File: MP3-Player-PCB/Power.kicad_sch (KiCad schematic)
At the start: 43 parts, among them J201 Conn_01x02_Socket, J202 USB_C_Receptacle_USB2.0_16P, U201 BQ24259, U202 USBLC6-2SC6, U203 TPS7A2033PDBVR, U204 TPS7A2033PDBVR

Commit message: Fixed all ERC errors
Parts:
- renumbered C216 to C212, C217 to C213, C212 to C214, C213 to C215, C214 to C216, C215 to C217, R215 to R214, R214 to R215
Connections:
- net +VSYS: no longer C213.1, C214.1, FB201.2, U203.1 (IN), U203.3 (EN)
- new net +VSYS_FILT: C213.1, C214.1, FB201.2, U203.1 (IN), U203.3 (EN)

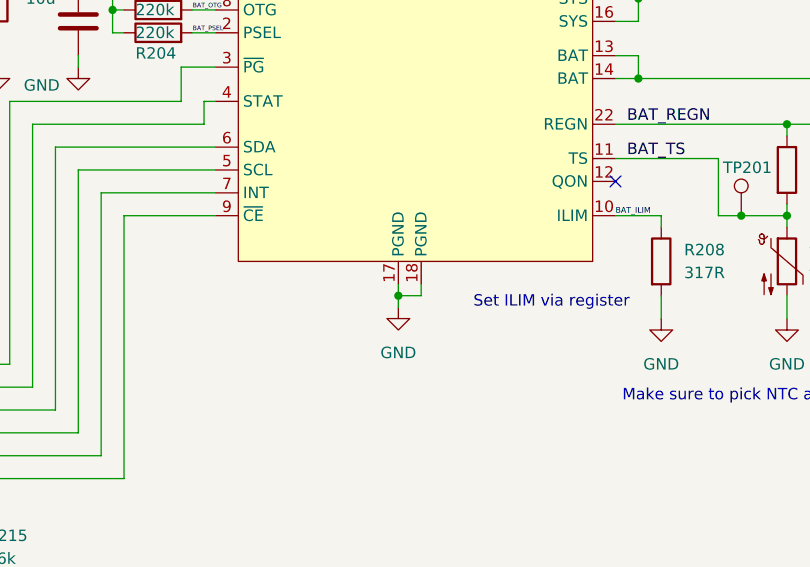
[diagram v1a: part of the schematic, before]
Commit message: Fixed all import change from schematic errors and warnings
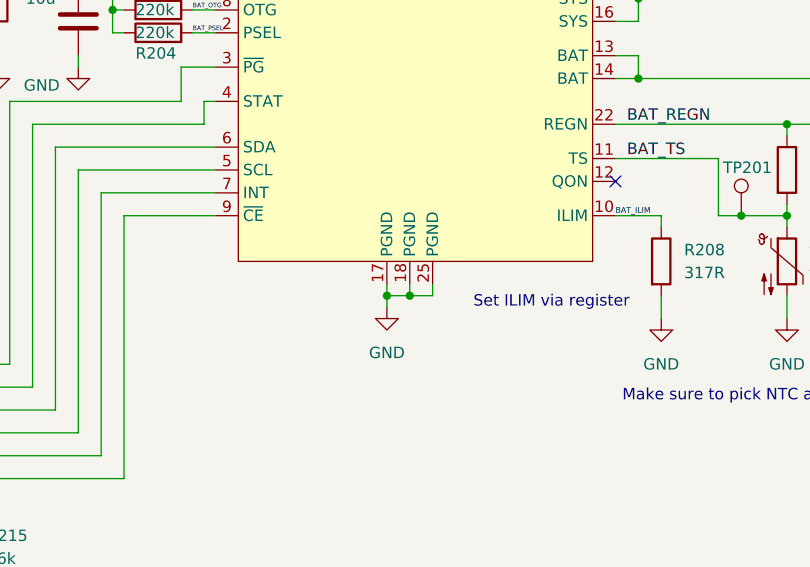
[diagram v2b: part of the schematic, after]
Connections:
- net GND: now also U201.25 (PGND)
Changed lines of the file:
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@@
 	)
 	(junction
-		(at 148.59 73.66)
+		(at 147.32 73.66)
 		(diameter 0)
 		(color 0 0 0 0)
@@
 	)
 	(junction
+		(at 149.86 73.66)
+		(diameter 0)
+		(color 0 0 0 0)
+	)
+	(junction
 		(at 73.66 71.12)
 		(diameter 0)
@@
 	(wire
 		(pts
-			(xy 148.59 73.66) (xy 148.59 74.93)
+			(xy 147.32 73.66) (xy 147.32 74.93)
 		)
 		(stroke
@@
 	(wire
 		(pts
+			(xy 152.4 72.39) (xy 152.4 73.66)
+		)
+		(stroke
+			(width 0)
+			(type default)
+		)
+	)
+	(wire
+		(pts
 			(xy 118.11 44.45) (xy 116.84 44.45)
 		)
@@
 	(wire
 		(pts
-			(xy 151.13 73.66) (xy 148.59 73.66)
+			(xy 149.86 73.66) (xy 147.32 73.66)
 		)
 		(stroke
@@
 	(wire
 		(pts
-			(xy 148.59 72.39) (xy 148.59 73.66)
+			(xy 147.32 72.39) (xy 147.32 73.66)
 		)
 		(stroke
@@
 	(wire
 		(pts
-			(xy 151.13 72.39) (xy 151.13 73.66)
+			(xy 149.86 72.39) (xy 149.86 73.66)
 		)
 		(stroke
@@
 	(wire
 		(pts
+			(xy 152.4 73.66) (xy 149.86 73.66)
+		)
+		(stroke
+			(width 0)
+			(type default)
+		)
+	)
+	(wire
+		(pts
 			(xy 186.69 30.48) (xy 190.5 30.48)
 		)
@@
 		(pin "2"
 		)
+		(pin "25"
+		)
 		(instances
 			(project ""
@@
 	(symbol
 		(lib_id "power:GND")
-		(at 148.59 74.93 0)
+		(at 147.32 74.93 0)
 		(unit 1)
 		(exclude_from_sim no)
@@
 		(fields_autoplaced yes)
 		(property "Reference" "#PWR0217"
-			(at 148.59 81.28 0)
+			(at 147.32 81.28 0)
 			(effects
 				(font
@@
 		)
 		(property "Value" "GND"
-			(at 148.59 80.01 0)
+			(at 147.32 80.01 0)
 			(effects
 				(font
@@
 		)
 		(property "Footprint" ""
-			(at 148.59 74.93 0)
+			(at 147.32 74.93 0)
 			(effects
 				(font
@@
 		)
 		(property "Datasheet" ""
-			(at 148.59 74.93 0)
+			(at 147.32 74.93 0)
 			(effects
 				(font
@@
 		)
 		(property "Description" "Power symbol creates a global label with name \"GND\" , ground"
-			(at 148.59 74.93 0)
+			(at 147.32 74.93 0)
 			(effects
 				(font

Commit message: Much better initial layout
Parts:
- C201, C202, C204: footprint Capacitor_SMD:C_0603_1608Metric -> Capacitor_SMD:C_0402_1005Metric
- C203, C209, C211, C212, C213: footprint Capacitor_SMD:C_0805_2012Metric -> Capacitor_SMD:C_0603_1608Metric
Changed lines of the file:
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@@
 			)
 		)
-		(property "Footprint" "Capacitor_SMD:C_0805_2012Metric"
+		(property "Footprint" "Capacitor_SMD:C_0603_1608Metric"
 			(at 44.1452 148.59 0)
 			(effects
@@
 			)
 		)
-		(property "Footprint" "Capacitor_SMD:C_0805_2012Metric"
+		(property "Footprint" "Capacitor_SMD:C_0603_1608Metric"
 			(at 26.3652 148.59 0)
 			(effects
@@
 			)
 		)
-		(property "Footprint" "Capacitor_SMD:C_0805_2012Metric"
+		(property "Footprint" "Capacitor_SMD:C_0603_1608Metric"
 			(at 113.9952 46.99 0)
 			(effects
@@
 			)
 		)
-		(property "Footprint" "Capacitor_SMD:C_0805_2012Metric"
+		(property "Footprint" "Capacitor_SMD:C_0603_1608Metric"
 			(at 213.0552 64.77 0)
 			(effects
@@
 			)
 		)
-		(property "Footprint" "Capacitor_SMD:C_0805_2012Metric"
+		(property "Footprint" "Capacitor_SMD:C_0603_1608Metric"
 			(at 96.2152 40.64 0)
 			(effects
@@
 			)
 		)
-		(property "Footprint" "Capacitor_SMD:C_0603_1608Metric"
+		(property "Footprint" "Capacitor_SMD:C_0402_1005Metric"
 			(at 68.2752 40.64 0)
 			(effects
@@
 			)
 		)
-		(property "Footprint" "Capacitor_SMD:C_0603_1608Metric"
+		(property "Footprint" "Capacitor_SMD:C_0402_1005Metric"
 			(at 182.88 35.8648 0)
 			(effects
@@
 			)
 		)
-		(property "Footprint" "Capacitor_SMD:C_0603_1608Metric"
+		(property "Footprint" "Capacitor_SMD:C_0402_1005Metric"
 			(at 84.7852 40.64 0)
 			(effects

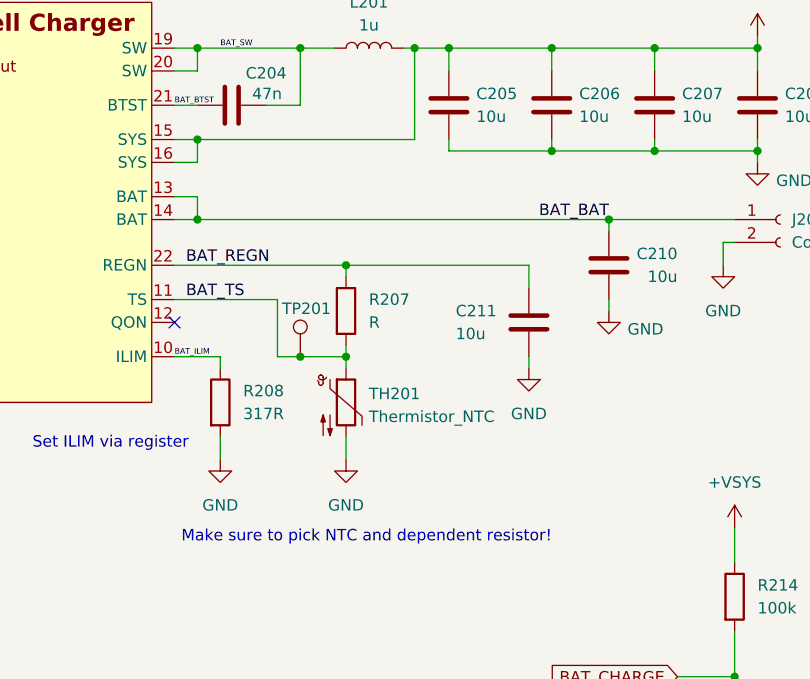
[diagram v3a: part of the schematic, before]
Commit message: Routing more mcu signals
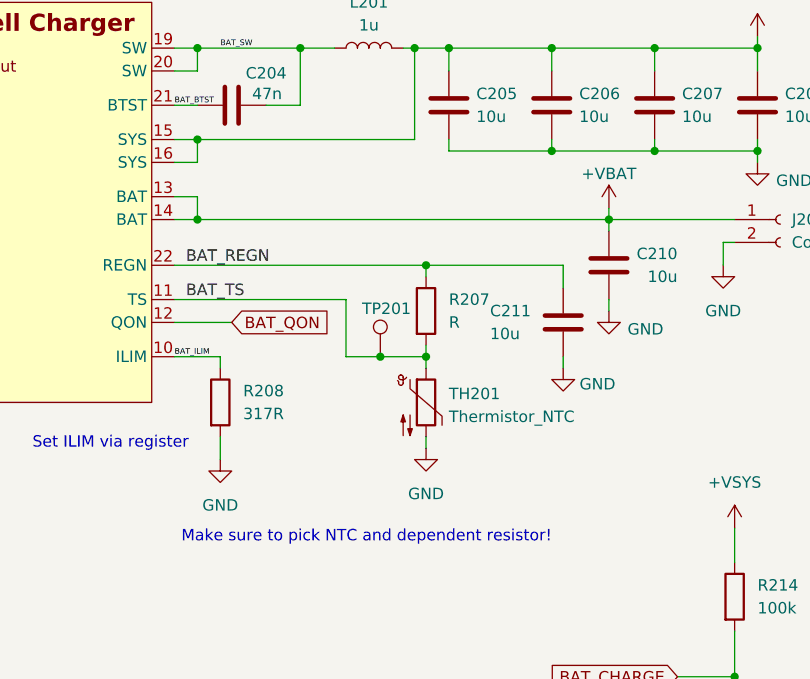
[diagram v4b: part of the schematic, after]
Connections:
- net BAT_QON: now reaches U201.12 (QON)
- net BAT_BAT renamed +VBAT
- no-connect marks 3 -> 2
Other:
- moved on the sheet: C211, R207, TH201, TP201

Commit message: Changing JST connector footprint to fit next to usb
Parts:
- J201: footprint Connector_JST:JST_EH_S2B-EH_1x02_P2.50mm_Horizontal -> Connector_JST:JST_GH_SM02B-GHS-TB_1x02-1MP_P1.25mm_Horizontal
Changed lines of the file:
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@@
 			)
 		)
-		(property "Footprint" "Connector_JST:JST_EH_S2B-EH_1x02_P2.50mm_Horizontal"
+		(property "Footprint" "Connector_JST:JST_GH_SM02B-GHS-TB_1x02-1MP_P1.25mm_Horizontal"
 			(at 240.03 49.53 0)
 			(effects

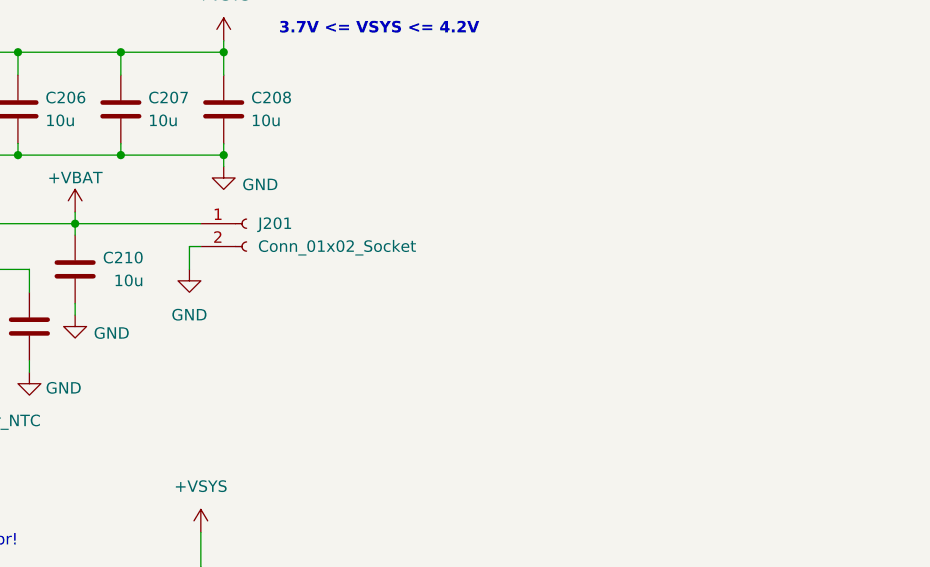
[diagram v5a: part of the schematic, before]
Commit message: Routed VBAT power trace in 3rd layer
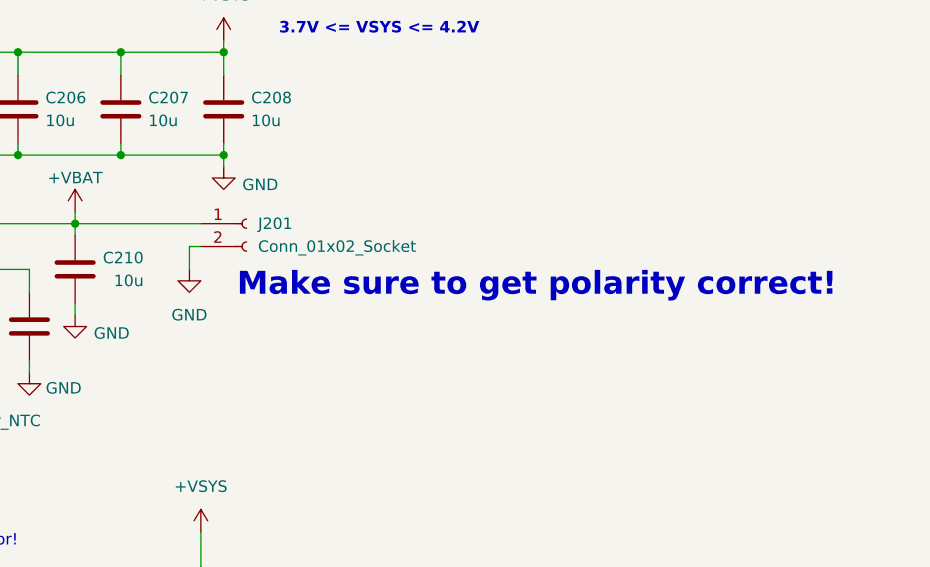
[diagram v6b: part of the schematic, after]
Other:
- note added: "Make sure to get polarity correct!"
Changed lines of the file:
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@@
+		)
+	)
+	(text "Make sure to get polarity correct!"
+		(exclude_from_sim no)
+		(at 272.288 56.388 0)
+		(effects
+			(font
+				(size 2.54 2.54)
+				(thickness 0.254)
+				(bold yes)
+			)
 		)
 	)

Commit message: Assigning JLCPCB part #'s
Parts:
- C201, C202: JLCPCB Part # (none) -> C1525
- C203, C209, C211, C212, C213: JLCPCB Part # (none) -> C19702
- C204: JLCPCB Part # (none) -> C82219
- C205, C206, C207, C208, C210, C214, C215, C216, C217: JLCPCB Part # (none) -> C15850
- FB201: JLCPCB Part # (none) -> C5671
- J201: JLCPCB Part # (none) -> C189893
- J202: footprint Connector_USB:USB_C_Receptacle_GCT_USB4105-xx-A_16P_TopMnt_Horizontal -> Connector_USB:USB_C_Receptacle_HRO_TYPE-C-31-M-12; JLCPCB Part # (none) -> C165948
- L201: JLCPCB Part # (none) -> C43388
- R201: JLCPCB Part # (none) -> C15402
- R202, R203, R204: JLCPCB Part # (none) -> C25546
- R205, R206: JLCPCB Part # (none) -> C25905
- R209, R210, R213, R215: JLCPCB Part # (none) -> C25796
- R211, R212: JLCPCB Part # (none) -> C25531
- R214: JLCPCB Part # (none) -> C25741
- R216: JLCPCB Part # (none) -> C25764
- TH201: JLCPCB Part # (none) -> C700814
- TP201: now left out of the parts list
- U201: JLCPCB Part # (none) -> C473366
- U202: JLCPCB Part # (none) -> C7519
- U203, U204: JLCPCB Part # (none) -> C2862740

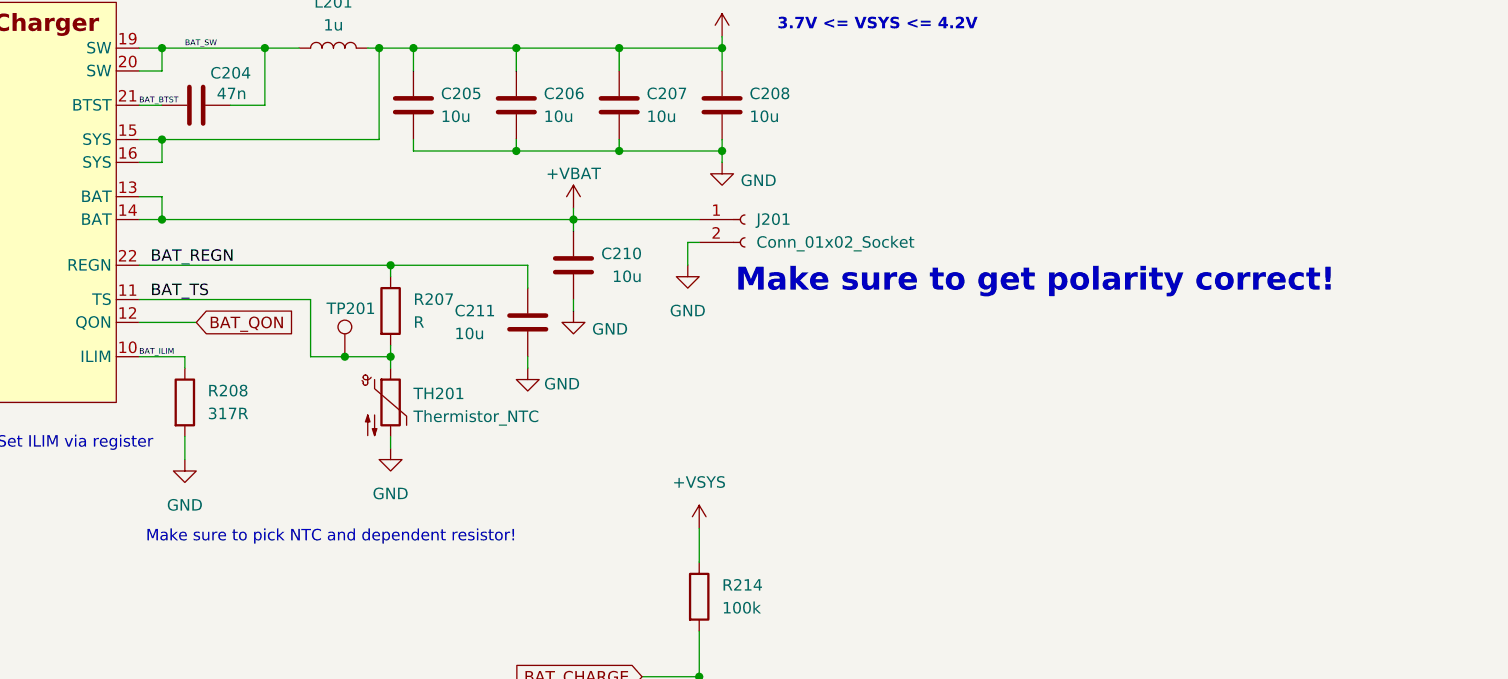
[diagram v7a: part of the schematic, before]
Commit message: Added 5.25k resistor to thermistor divider network as per BQ24259 datasheet
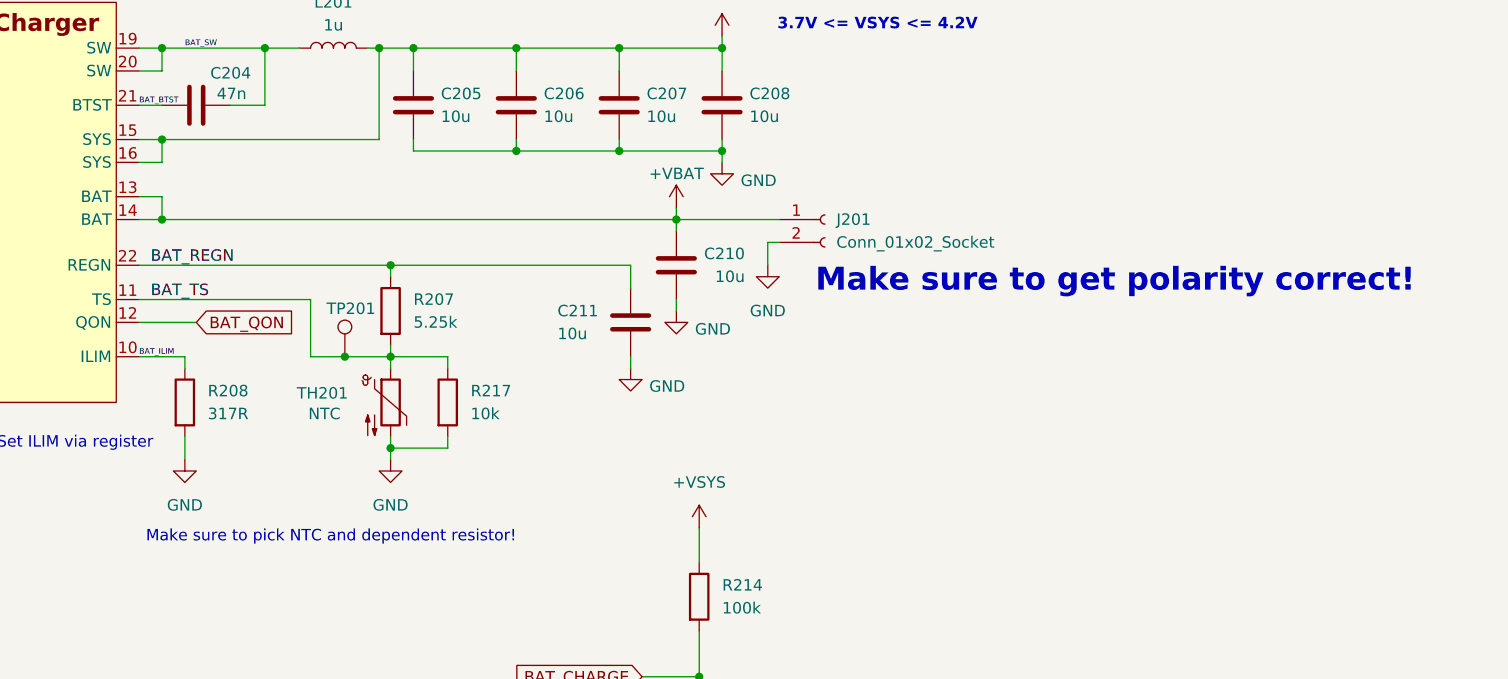
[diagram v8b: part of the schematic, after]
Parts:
- added R217: 10k, Resistor_SMD:R_0402_1005Metric, symbol Device:R
- R207: value R -> 5.25k
- R211, R212: JLCPCB Part # C25531 -> C25744
- TH201: value Thermistor_NTC -> NTC
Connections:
- net BAT_TS: now also R217.1
- net GND: now also R217.2
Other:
- moved on the sheet: C210, C211, J201
